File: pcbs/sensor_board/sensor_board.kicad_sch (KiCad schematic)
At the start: 41 parts, among them J1 1.5mm, J2 2.5mm, J3 2.5mm, J4 1.5 mm, J5 RJ45, J6 Conn_01x06, Q1 220mA / 50V, Q2 220mA / 50V, Q3 220mA / 50V, U1 8-28V in / 5V 5W out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

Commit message: sensor board version 1.1
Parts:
- D1: JLCPCB C125085 -> C125086; JLCPCBURL https://jlcpcb.com/partdetail/LiteOn-LTSTC150KGKT/C125085 -> https://jlcpcb.com/partdetail/LiteOn-LTSTC150KRKT/C125086
- R1: JLCPCB C4410 -> (none); JLCPCBURL https://jlcpcb.com/partdetail/4817-1206W4F1001T5E/C4410 -> (none)
- R11, R12, R13, R14: JLCPCB C17902 -> (none); JLCPCBURL https://jlcpcb.com/partdetail/18590-1206W4F1002T5E/C17902 -> (none)
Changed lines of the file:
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@@
 	)
 	(junction
-		(at 251.46 199.39)
-		(diameter 0)
-		(color 0 0 0 0)
-	)
-	(junction
 		(at 350.52 129.54)
 		(diameter 0)
@@
 	(wire
 		(pts
-			(xy 251.46 199.39) (xy 251.46 201.93)
-		)
-		(stroke
-			(width 0)
-			(type default)
-		)
-	)
-	(wire
-		(pts
 			(xy 304.8 52.07) (xy 304.8 50.8)
 		)
@@
 	(wire
 		(pts
-			(xy 251.46 198.12) (xy 251.46 199.39)
+			(xy 251.46 199.39) (xy 251.46 201.93)
 		)
 		(stroke
@@
 			)
 		)
-		(property "JLCPCB" "C4410"
-			(at 312.42 171.45 0)
-			(effects
-				(font
-					(size 1.27 1.27)
-				)
-				(hide yes)
-			)
-		)
-		(property "JLCPCBURL" "https://jlcpcb.com/partdetail/4817-1206W4F1001T5E/C4410"
-			(at 312.42 171.45 0)
-			(effects
-				(font
-					(size 1.27 1.27)
-				)
-				(hide yes)
-			)
-		)
 		(pin "1"
 		)
@@
 			)
 		)
-		(property "JLCPCB" "C125085"
+		(property "JLCPCB" "C125086"
 			(at 58.42 63.5 0)
 			(effects
@@
 			)
 		)
-		(property "JLCPCBURL" "https://jlcpcb.com/partdetail/LiteOn-LTSTC150KGKT/C125085"
+		(property "JLCPCBURL" "https://jlcpcb.com/partdetail/LiteOn-LTSTC150KRKT/C125086"
 			(at 58.42 63.5 0)
 			(effects
@@
 			)
 		)
-		(property "JLCPCB" "C17902"
-			(at 219.71 63.5 0)
-			(effects
-				(font
-					(size 1.27 1.27)
-				)
-				(hide yes)
-			)
-		)
-		(property "JLCPCBURL" "https://jlcpcb.com/partdetail/18590-1206W4F1002T5E/C17902"
-			(at 219.71 63.5 0)
-			(effects
-				(font
-					(size 1.27 1.27)
-				)
-				(hide yes)
-			)
-		)
 		(pin "1"
 		)
@@
 			)
 		)
-		(property "JLCPCB" "C17902"
-			(at 219.71 71.12 0)
-			(effects
-				(font
-					(size 1.27 1.27)
-				)
-				(hide yes)
-			)
-		)
-		(property "JLCPCBURL" "https://jlcpcb.com/partdetail/18590-1206W4F1002T5E/C17902"
-			(at 219.71 71.12 0)
-			(effects
-				(font
-					(size 1.27 1.27)
-				)
-				(hide yes)
-			)
-		)
 		(pin "1"
 		)
@@
 			)
 		)
-		(property "JLCPCB" "C17902"
-			(at 215.9 50.8 0)
-			(effects
-				(font
-					(size 1.27 1.27)
-				)
-				(hide yes)
-			)
-		)
-		(property "JLCPCBURL" "https://jlcpcb.com/partdetail/18590-1206W4F1002T5E/C17902"
-			(at 215.9 50.8 0)
-			(effects
-				(font
-					(size 1.27 1.27)
-				)
-				(hide yes)
-			)
-		)
 		(pin "1"
 		)
@@
 			(at 219.71 78.74 0)
 			(effects
-				(font
-					(size 1.27 1.27)
-				)
-				(hide yes)
-			)
-		)
-		(property "JLCPCB" "C17902"
-			(at 219.71 78.74 0)
-			(effects
-				(font
-					(size 1.27 1.27)
-				)
-				(hide yes)
-			)
-		)
-		(property "JLCPCBURL" "https://jlcpcb.com/partdetail/18590-1206W4F1002T5E/C17902"
-			(at 219.71 78.74 0)
-			(effects

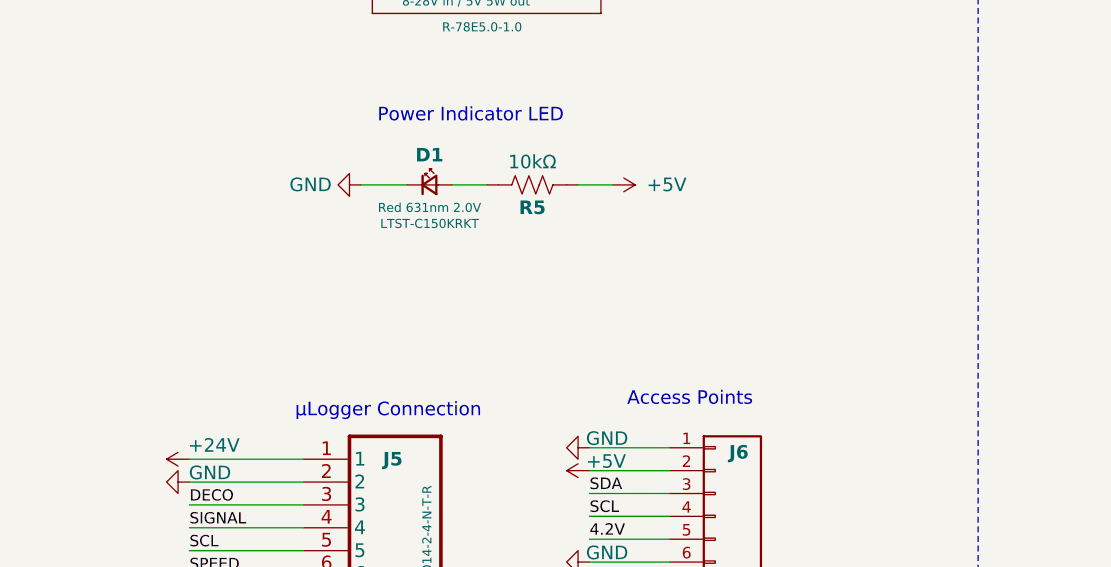
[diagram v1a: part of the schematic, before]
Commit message: update controller board to version 1.1 - i2c level shifting back to mosfets
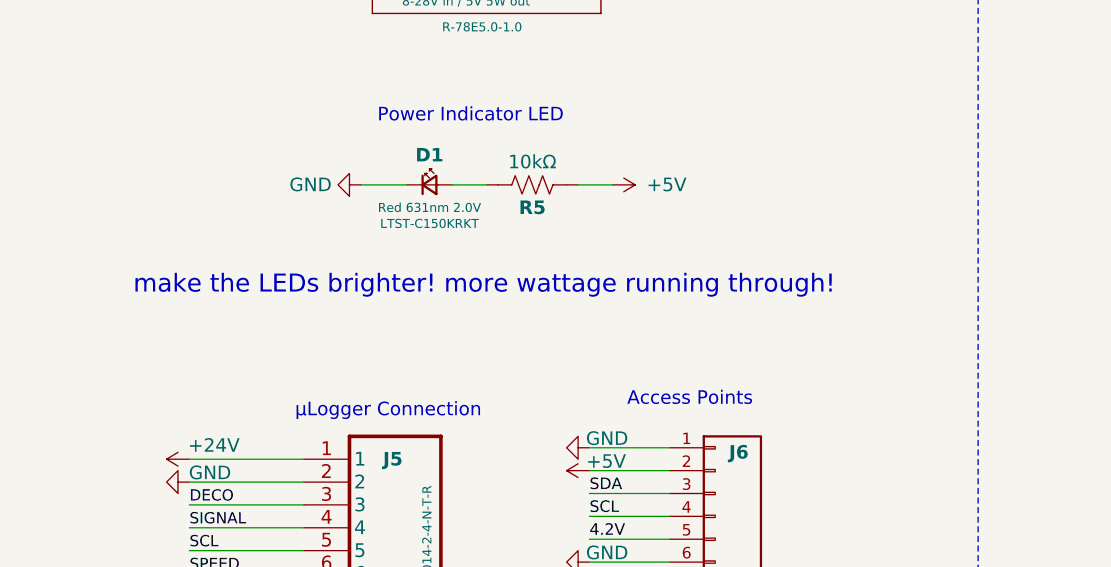
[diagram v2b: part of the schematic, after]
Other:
- note added: "make the LEDs brighter! more wattage running through!"
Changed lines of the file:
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@@
+		)
+	)
+	(text "make the LEDs brighter! more wattage running through!"
+		(exclude_from_sim no)
+		(at 64.516 74.676 0)
+		(effects
+			(font
+				(size 2 2)
+				(color 255 0 0 1)
+			)
 		)
 	)

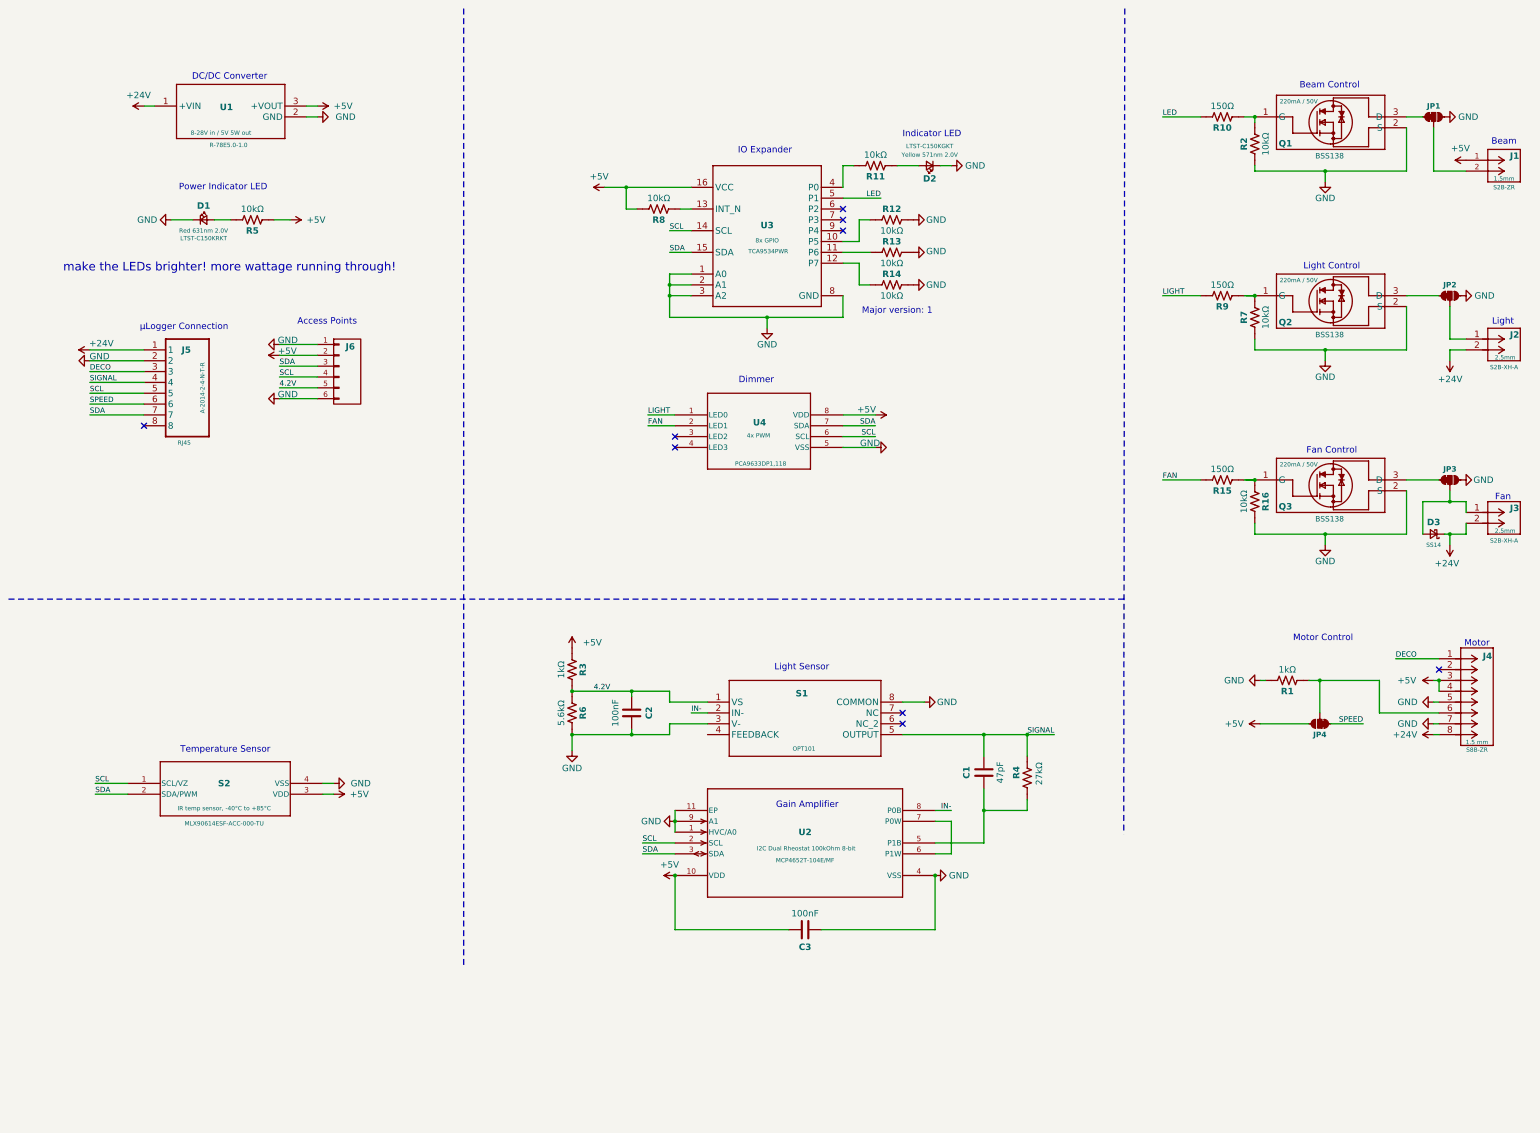
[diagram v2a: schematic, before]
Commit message: upgrade to version 1.2
 - lower resistor for indicator LEDs (brighter)
 - better position for indicator LEDs (left/right)
 - io expander beam/indicator LED switched (=backwards compatibility)
 - switch contacts for the fan (opposite to the lights)
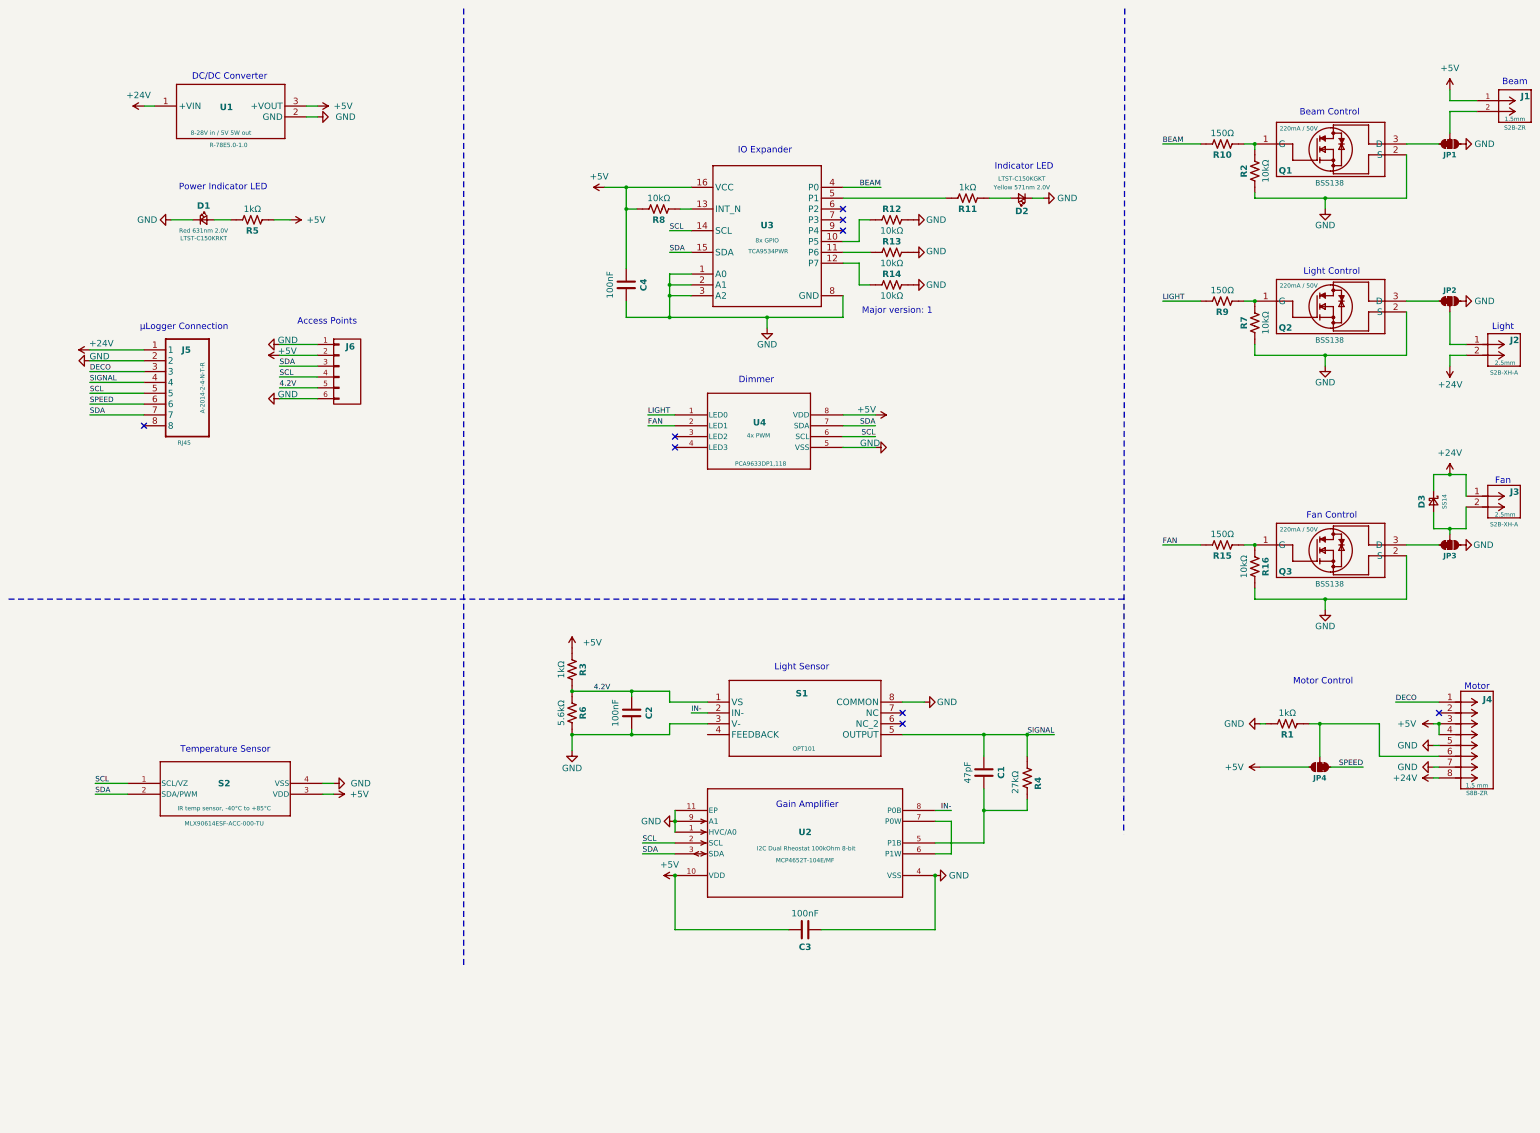
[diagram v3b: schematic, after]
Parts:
- added C4: 100nF, footprints:C_0603, symbol symbols:C_0603
- R11, R5: value 10kΩ -> 1kΩ
- R4: footprint footprints:R_0603 -> footprints:R_1206
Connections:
- net +24V: now also J3.1; no longer J3.2
- net +5V: now also C4.1
- net GND: now also C4.2
- net SIGNAL: now also C1.1, R4.1; no longer C1.2, R4.2
- net at D3.2 (A), JP3.2 (B): now also J3.2; no longer J3.1
- net at R11.2: now also U3.5 (P1); no longer U3.4 (P0)
- net LED renamed BEAM
- net BEAM: now also U3.4 (P0); no longer U3.5 (P1)
- new net: C1.2, R4.2, U2.5 (P1B)
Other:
- note removed: "make the LEDs brighter! more wattage running through!"
- moved on the sheet: C1, D2, D3, J1, J2, J3, J4, JP1, JP2, JP3, JP4, Q1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

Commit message: sensor board version 1.3
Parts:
- removed U2: I2C Dual Rheostat 100kOhm 8-bit, footprints:DFN10_3x3MC, symbol symbols:DigiPot_MCP4652T_100kOhm_MF
- added J7, J8: Conn_01x02, footprints:PIN_HEADERS_1X02, symbol symbols:PINHD-1X2
- added U4: 100 kOhm, footprints:SOT-363_TSSOP6_SC88, symbol symbols:DigiPot_AD5246BKSZ100
- added U5: 100 kOhm, footprints:SOT-363_TSSOP6_SC88, symbol symbols:DigiPot_MCP4017T-104E
- R4: value 27kΩ -> 10kΩ; JLCPCB C403122 -> C17902; JLCPCBURL https://jlcpcb.com/partdetail/PANASONIC-ERJ3EKF2702V/C403122 -> https://jlcpcb.com/partdetail/18590-1206W4F1002T5E/C17902
- R5: JLCPCB C191124 -> (none); JLCPCBURL https://jlcpcb.com/partdetail/PANASONIC-ERJ3EKF1002V/C19112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 -> (none)
- R8: JLCPCB (none) -> C191124; JLCPCBURL (none) -> https://jlcpcb.com/partdetail/PANASONIC-ERJ3EKF1002V/C19112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
- renumbered U3 to U2, U4 to U3
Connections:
- net +5V: now also U4.1 (VDD), U5.1 (VDD)
- net GND: now also J8.2 (Pin_2), U4.2 (GND), U5.2 (VSS)
- net SCL: now also U4.3 (SCL), U5.3 (SCL)
- net SDA: now also U4.4 (SDA), U5.4 (SDA)
- net SIGNAL: now also J7.1 (Pin_1), J8.1 (Pin_1)
- net at C1.2, R4.2: now also U4.6 (B)
- net IN- renamed AMP
- net AMP: now also J7.2 (Pin_2), U5.5 (B)
- new net: U4.5 (W), U5.6 (W)
- no-connect marks 9 -> 10
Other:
- note added: "Gain Amplification"
- note removed: "Gain Amplifier"
- moved on the sheet: C1, C2, C3, R3, R4, R6, S1

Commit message: fix capacitor placaement on sensor board (IN- to SIGNAL)
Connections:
- net AMP: now also C1.1
- net SIGNAL: now also C1.2; no longer C1.1
- net at R4.2, U4.6 (B): no longer C1.2
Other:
- moved on the sheet: C1, C2, R3, R4, R6, S1

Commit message: add signal stabilizing capacitors to controller and sensor boards
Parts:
- added R17: 150Ω, footprints:R_0603, symbol symbols:R_US_0603
- C1: value 47pF -> 100pF; JLCPCB C1671 -> C14858; JLCPCBURL https://jlcpcb.com/partdetail/2023-CL10C470JB8NNNC/C1671 -> https://jlcpcb.com/partdetail/15530-CL10C101JB8NNNC/C14858
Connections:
- net SIGNAL: now also R17.1; no longer C1.2, J7.1 (Pin_1), R4.1, S1.5 (OUTPUT)
- new net OUTPUT: C1.2, J7.1 (Pin_1), R17.2, R4.1, S1.5 (OUTPUT)
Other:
- moved on the sheet: C2, C3, R3, R6

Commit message: sensor board version 1.4
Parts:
- removed R17: 150Ω, footprints:R_0603, symbol symbols:R_US_0603
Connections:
- net OUTPUT is gone; now on net SIGNAL: C1.2, J7.1 (Pin_1), R4.1, S1.5 (OUTPUT)
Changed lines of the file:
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@@
 	(wire
 		(pts
-			(xy 255.27 181.61) (xy 264.16 181.61)
-		)
-		(stroke
-			(width 0)
-			(type default)
-		)
-	)
-	(wire
-		(pts
 			(xy 184.15 201.93) (xy 186.69 201.93)
 		)
@@
 	(wire
 		(pts
-			(xy 240.03 181.61) (xy 245.11 181.61)
+			(xy 240.03 181.61) (xy 256.54 181.61)
 		)
 		(stroke
@@
 		)
 	)
-	(label "OUTPUT"
+	(label "SIGNAL"
 		(at 76.2 114.3 0)
 		(effects
@@
 	)
 	(label "SIGNAL"
-		(at 264.16 181.61 180)
+		(at 256.54 181.61 180)
 		(effects
 			(font
@@
 		)
 	)
-	(label "OUTPUT"
-		(at 240.03 167.64 0)
-		(effects
-			(font
-				(size 1.27 1.27)
-			)
-			(justify left bottom)
-		)
-	)
 	(label "SDA"
 		(at 33.02 198.12 0)
@@
 					(unit 1)
 				)
-			)
-		)
-	)
-	(symbol
-		(lib_id "symbols:R_US_0603")
-		(at 250.19 181.61 0)
-		(unit 1)
-		(exclude_from_sim no)
-		(in_bom yes)
-		(on_board yes)
-		(dnp no)
-		(property "Reference" "R17"
-			(at 250.19 184.15 0)
-			(effects
-				(font
-					(size 1.5 1.5)
-					(thickness 0.3)
-					(bold yes)
-				)
-			)
-		)
-		(property "Value" "150Ω"
-			(at 250.19 179.07 0)
-			(effects
-				(font
-					(size 1.5 1.5)
-				)
-			)
-		)
-		(property "Footprint" "footprints:R_0603"
-			(at 251.206 181.864 90)
-			(effects
-				(font
-					(size 1.27 1.27)
-				)
-				(hide yes)
-			)
-		)
-		(property "Datasheet" "~"
-			(at 250.19 181.61 0)
-			(effects
-				(font
-					(size 1.27 1.27)
-				)
-				(hide yes)
-			)
-		)
-		(property "Description" "Resistor, US symbol"
-			(at 250.19 181.61 0)
-			(effects
-				(font
-					(size 1.27 1.27)
-				)
-				(hide yes)
-			)
-		)
-		(pin "1"
-		)
-		(pin "2"
-		)
-		(instances
-			(project "sensor_board"
-				(path "/2e363057-5f2b-4813-9b6e-20c9934d11ef"
-					(reference "R17")
-					(unit 1)
-				)

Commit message: update sensor board with 1M potentiometer
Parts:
- removed U4: 100 kOhm, footprints:SOT-363_TSSOP6_SC88, symbol symbols:DigiPot_AD5246BKSZ100
- added C5: 100nF, footprints:C_0603, symbol symbols:C_0603
- added U4: 1 MOhm, footprints:14-SOIC, symbol symbols:DigiPot_AD5241BRZ_1MOhm
- JP1, JP2, JP3, JP4: value ~ -> (none)
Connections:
- net +5V: now also R14.2, C5.1, U4.1 (A1), U4.4 (VDD), U4.5 (SHDN*)
- net GND: now also C5.2, U4.10 (DGND), U4.11 (VSS), U4.8 (AD0), U4.9 (AD1); no longer R14.2
- net SCL: now also U4.6 (SCL)
- net SDA: now also U4.7 (SDA)
- net at R4.2: now also U4.3 (B1)
- net at U5.6 (W): now also U4.2 (W1)
- no-connect marks 10 -> 13
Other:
- note added: "Major version: 2"
- note added: "this was 10 kOhm originally (in 1.4) but has now moved to 56 kOhm for the other LEDs (600nm and 880nm) but if we have a 1 MOhm secondary digipot in there, should go back to 10 kOhm! (so total range is 10 kOhm to 1.1 MOhm) Note: 1.4 version PCBs were retroactively upgraded to 56 kOhm"
- note removed: "Major version: 1"
- moved on the sheet: C1, C3, R4, U5
